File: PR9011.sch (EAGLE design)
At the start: 65 parts, among them J1 M3_SCREW_POST, SW1 SPST_TACT-KMR2, Y1 32.768kHz

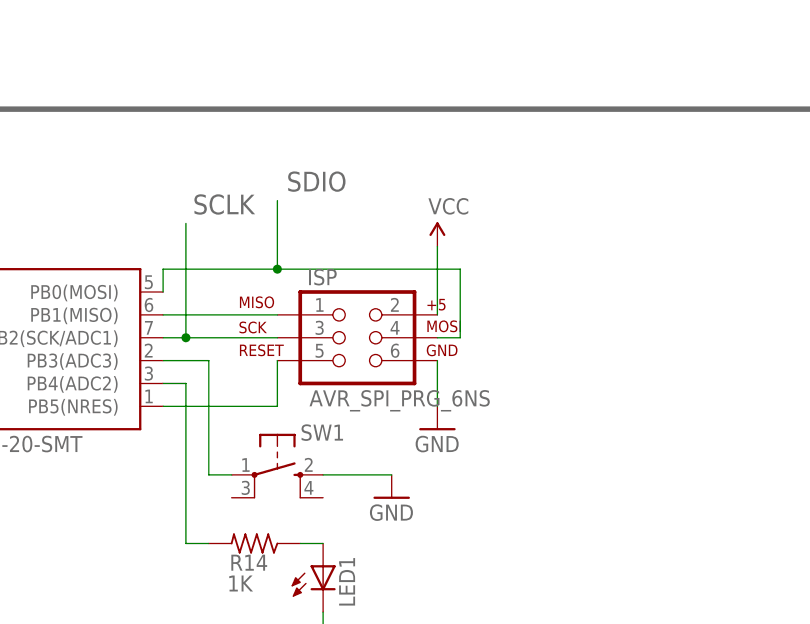
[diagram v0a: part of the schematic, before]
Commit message: Updated SCH
Updated Pullup Resist & Decoupling Vals
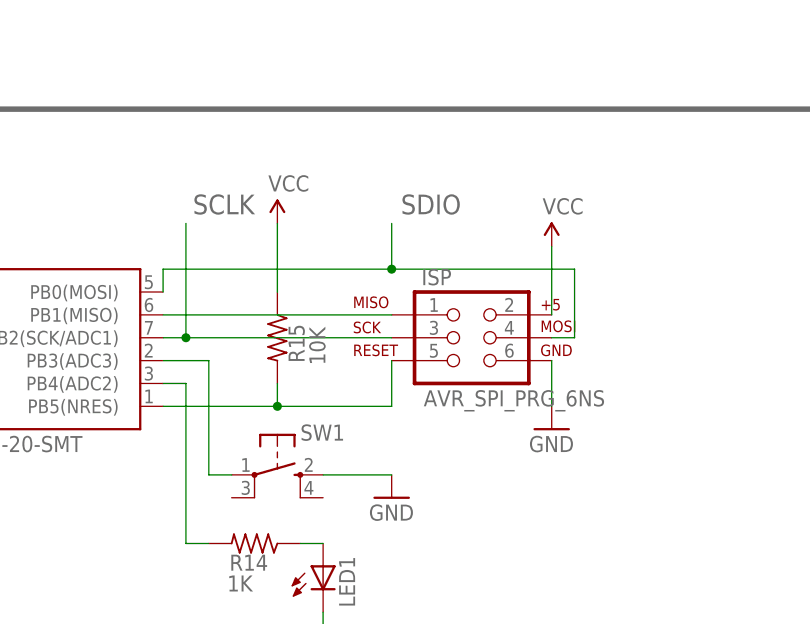
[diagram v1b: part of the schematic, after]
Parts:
- added R15: 10K, resistor:R-US_R0603
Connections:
- net PB5: now also R15.2
- net VCC: now also R15.1
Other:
- moved on the sheet: ISP
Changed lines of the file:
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@@
 <part name="VARI" library="coilcraft-trimmer" deviceset="L-TRIM" device=""/>
 <part name="GND33" library="SparkFun-Aesthetics" deviceset="GND" device=""/>
+<part name="R15" library="resistor" deviceset="R-US_" device="R0603" value="10K"/>
+<part name="SUPPLY1" library="SparkFun-Aesthetics" deviceset="VCC" device=""/>
 </parts>
 <sheets>
@@
 <attribute name="NAME" x="226.06" y="34.798" size="1.778" layer="95" rot="R180"/>
 </instance>
-<instance part="ISP" gate="G$1" x="208.28" y="127"/>
+<instance part="ISP" gate="G$1" x="220.98" y="127"/>
 <instance part="LED1" gate="G$1" x="205.74" y="101.6"/>
 <instance part="GND30" gate="1" x="205.74" y="91.44"/>
-<instance part="SUPPLY9" gate="G$1" x="218.44" y="137.16"/>
-<instance part="GND32" gate="1" x="218.44" y="116.84"/>
+<instance part="SUPPLY9" gate="G$1" x="231.14" y="137.16"/>
+<instance part="GND32" gate="1" x="231.14" y="116.84"/>
 <instance part="R14" gate="G$1" x="198.12" y="104.14" smashed="yes" rot="R180">
 <attribute name="NAME" x="195.326" y="101.1174" size="1.778" layer="95"/>
@@
 <instance part="VARI" gate="G$1" x="17.78" y="25.4"/>
 <instance part="GND33" gate="1" x="17.78" y="15.24"/>
+<instance part="R15" gate="G$1" x="200.66" y="127" smashed="yes" rot="R270">
+<attribute name="NAME" x="203.6826" y="124.206" size="1.778" layer="95" rot="R90"/>
+<attribute name="VALUE" x="205.994" y="123.952" size="1.778" layer="96" rot="R90"/>
+</instance>
+<instance part="SUPPLY1" gate="G$1" x="200.66" y="139.7"/>
 </instances>
 <busses>
@@
 <segment>
 <pinref part="ISP" gate="G$1" pin="6"/>
-<wire x1="218.44" y1="124.46" x2="218.44" y2="119.38" width="0.1524" layer="91"/>
+<wire x1="231.14" y1="124.46" x2="231.14" y2="119.38" width="0.1524" layer="91"/>
 <pinref part="GND32" gate="1" pin="GND"/>
 </segment>
@@
 <pinref part="MCU" gate="G$1" pin="PB2(SCK/ADC1)"/>
 <pinref part="ISP" gate="G$1" pin="3"/>
-<wire x1="200.66" y1="127" x2="190.5" y2="127" width="0.1524" layer="91"/>
+<wire x1="213.36" y1="127" x2="190.5" y2="127" width="0.1524" layer="91"/>
 <label x="191.262" y="140.716" size="2.1844" layer="95"/>
 <wire x1="190.5" y1="127" x2="187.96" y2="127" width="0.1524" layer="91"/>
@@
 </segment>
 <segment>
-<wire x1="220.98" y1="134.62" x2="220.98" y2="127" width="0.1524" layer="91"/>
+<wire x1="233.68" y1="134.62" x2="233.68" y2="127" width="0.1524" layer="91"/>
 <pinref part="ISP" gate="G$1" pin="4"/>
-<wire x1="220.98" y1="127" x2="218.44" y2="127" width="0.1524" layer="91"/>
-<label x="201.676" y="143.256" size="2.1844" layer="95"/>
+<wire x1="233.68" y1="127" x2="231.14" y2="127" width="0.1524" layer="91"/>
+<label x="214.376" y="140.716" size="2.1844" layer="95"/>
 <pinref part="MCU" gate="G$1" pin="PB0(MOSI)"/>
-<wire x1="220.98" y1="134.62" x2="200.66" y2="134.62" width="0.1524" layer="91"/>
-<wire x1="200.66" y1="134.62" x2="187.96" y2="134.62" width="0.1524" layer="91"/>
+<wire x1="233.68" y1="134.62" x2="213.36" y2="134.62" width="0.1524" layer="91"/>
+<wire x1="213.36" y1="134.62" x2="187.96" y2="134.62" width="0.1524" layer="91"/>
 <wire x1="187.96" y1="134.62" x2="187.96" y2="132.08" width="0.1524" layer="91"/>
-<wire x1="200.66" y1="134.62" x2="200.66" y2="142.24" width="0.1524" layer="91"/>
-<junction x="200.66" y="134.62"/>
+<wire x1="213.36" y1="134.62" x2="213.36" y2="139.7" width="0.1524" layer="91"/>
+<junction x="213.36" y="134.62"/>
 </segment>
 </net>
@@
 <segment>
 <pinref part="ISP" gate="G$1" pin="2"/>
-<wire x1="218.44" y1="137.16" x2="218.44" y2="129.54" width="0.1524" layer="91"/>
+<wire x1="231.14" y1="137.16" x2="231.14" y2="129.54" width="0.1524" layer="91"/>
 <pinref part="SUPPLY9" gate="G$1" pin="VCC"/>
 </segment>
@@
 <pinref part="C14" gate="G$1" pin="1"/>
 <wire x1="139.7" y1="139.7" x2="139.7" y2="137.16" width="0.1524" layer="91"/>
+</segment>
+<segment>
+<pinref part="R15" gate="G$1" pin="1"/>
+<wire x1="200.66" y1="132.08" x2="200.66" y2="139.7" width="0.1524" layer="91"/>
+<pinref part="SUPPLY1" gate="G$1" pin="VCC"/>
 </segment>
 </net>
@@
 <pinref part="ISP" gate="G$1" pin="5"/>
 <wire x1="187.96" y1="119.38" x2="200.66" y2="119.38" width="0.1524" layer="91"/>
-<wire x1="200.66" y1="119.38" x2="200.66" y2="124.46" width="0.1524" layer="91"/>
+<wire x1="200.66" y1="119.38" x2="213.36" y2="119.38" width="0.1524" layer="91"/>
+<wire x1="213.36" y1="119.38" x2="213.36" y2="124.46" width="0.1524" layer="91"/>
+<pinref part="R15" gate="G$1" pin="2"/>
+<wire x1="200.66" y1="121.92" x2="200.66" y2="119.38" width="0.1524" layer="91"/>
+<junction x="200.66" y="119.38"/>
 </segment>
 </net>
@@
 <pinref part="ISP" gate="G$1" pin="1"/>
 <pinref part="MCU" gate="G$1" pin="PB1(MISO)"/>
-<wire x1="187.96" y1="129.54" x2="200.66" y2="129.54" width="0.1524" layer="91"/>
-</segment>
-</net>
+<wire x1="187.96" y1="129.54" x2="213.36" y2="129.54" width="0.1524" layer="91"/>
+</segment>
+</net>

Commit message: Updated SCH
Updated SCH
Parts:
- C10: value 1.0uF -> 22nF
- C11: value 1.0uF -> 4.7uF
- C8: value 1.0uF -> .1uF
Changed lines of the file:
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@@
 <?xml version="1.0" encoding="utf-8"?>
 <!DOCTYPE eagle SYSTEM "eagle.dtd">
-<eagle version="6.6.0">
+<eagle version="7.2.0">
 <drawing>
 <settings>
@@
 <part name="C3" library="SparkFun-Capacitors" deviceset="1.0UF-25V-+80/-20(0805)" device="" value="1.0uF"/>
 <part name="GND21" library="SparkFun" deviceset="GND" device=""/>
-<part name="C8" library="SparkFun-Capacitors" deviceset="1.0UF-25V-+80/-20(0805)" device="" value="1.0uF"/>
-<part name="C10" library="SparkFun-Capacitors" deviceset="1.0UF-25V-+80/-20(0805)" device="" value="1.0uF"/>
-<part name="C11" library="SparkFun-Capacitors" deviceset="1.0UF-25V-+80/-20(0805)" device="" value="1.0uF"/>
+<part name="C8" library="SparkFun-Capacitors" deviceset="1.0UF-25V-+80/-20(0805)" device="" value=".1uF"/>
+<part name="C10" library="SparkFun-Capacitors" deviceset="1.0UF-25V-+80/-20(0805)" device="" value="22nF"/>
+<part name="C11" library="SparkFun-Capacitors" deviceset="1.0UF-25V-+80/-20(0805)" device="" value="4.7uF"/>
 <part name="C7" library="SparkFun-Capacitors" deviceset="1.0UF-25V-+80/-20(0805)" device="" value="1.0uF"/>
 <part name="GND16" library="SparkFun" deviceset="GND" device=""/>

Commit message: Updated SCH
Updated SCH
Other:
- note added: "PUBLIC RADIO PR9011 Development Board"
- note removed: "PUBLIC RADIO PR9010"
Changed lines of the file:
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@@
 <text x="160.02" y="76.2" size="2.54" layer="96">Audio Amplifier </text>
 <text x="157.48" y="144.78" size="2.54" layer="96">MCU</text>
-<text x="-27.94" y="162.56" size="3.81" layer="96">PUBLIC RADIO PR9010</text>
+<text x="-27.94" y="162.56" size="3.81" layer="96">PUBLIC RADIO PR9011
+Development Board </text>
 <text x="77.978" y="147.574" size="2.54" layer="96">GND Pads </text>
 </plain>
@@
 </schematic>
 </drawing>
+<compatibility>
+<note version="6.3" minversion="6.2.2" severity="warning">
+Since Version 6.2.2 text objects can contain more than one line,
+which will not be processed correctly with this version.
+</note>
+</compatibility>
 </eagle>

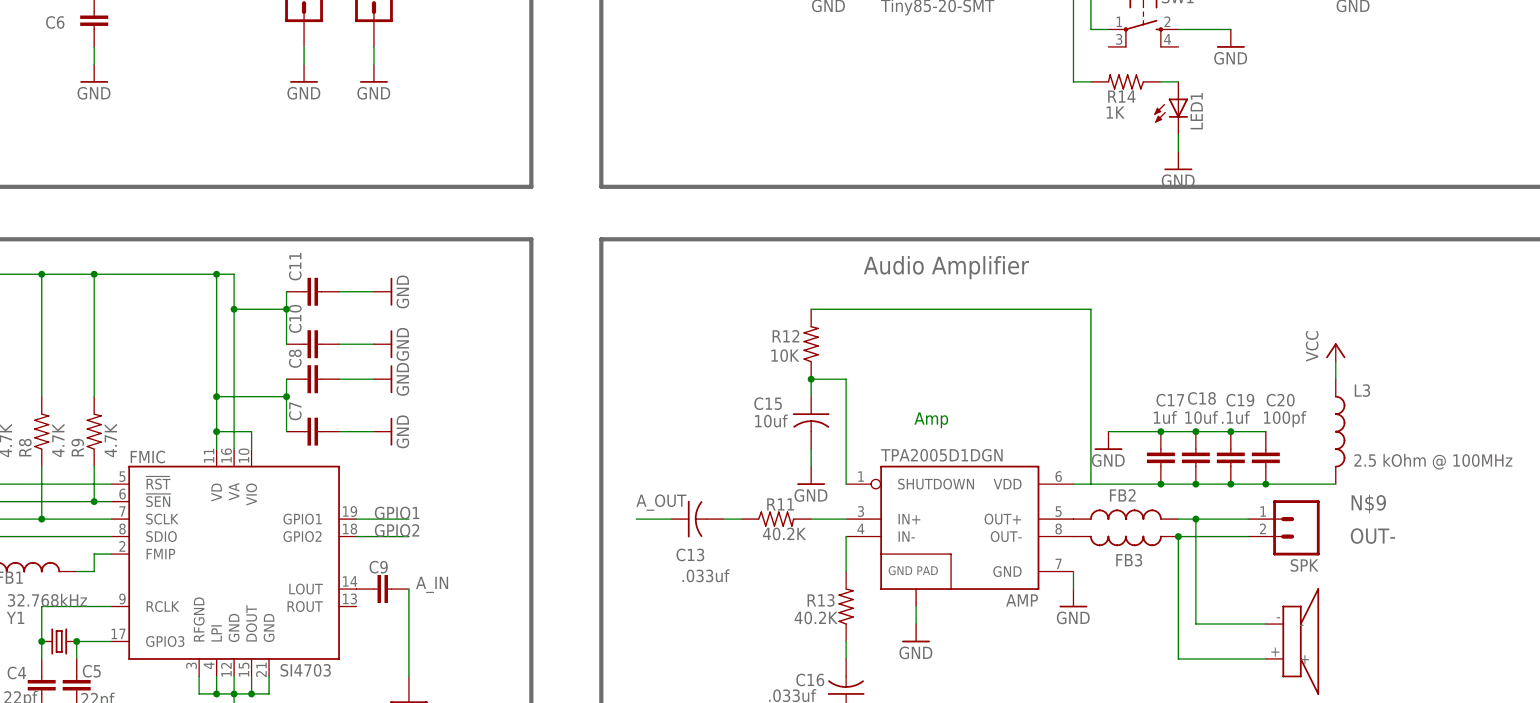
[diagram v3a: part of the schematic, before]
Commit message: Updated SCH
Updated SCH
JST
Fiducials
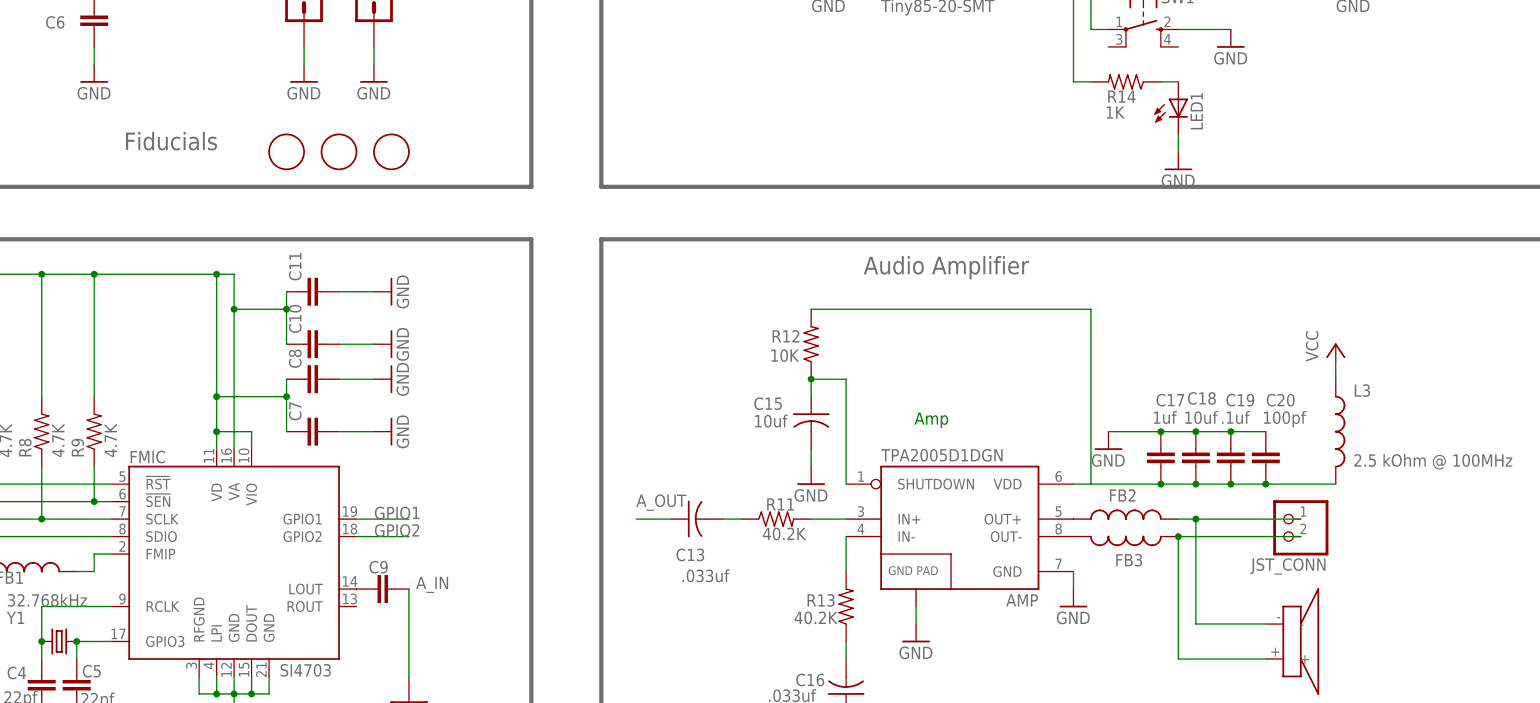
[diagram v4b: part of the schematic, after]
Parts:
- removed SPK: M02PTH3, SparkFun-Connectors:M02PTH3
- added JST_CONN: (no value), adafruit:JST_2PIN-SMT-RA
- added U$1, U$2, U$4: FIDUCIAL, adafruit:FIDUCIAL
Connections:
- net N$9: now also JST_CONN.2; no longer SPK.1
- net OUT-: now also JST_CONN.1; no longer SPK.2
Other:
- note added: "Fiducials"
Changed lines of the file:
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@@
 <?xml version="1.0" encoding="utf-8"?>
 <!DOCTYPE eagle SYSTEM "eagle.dtd">
-<eagle version="7.2.0">
+<eagle version="6.6.0">
 <drawing>
 <settings>
@@
 <part name="SW1" library="adafruit" deviceset="SPST_TACT" device="-KMR2"/>
 <part name="GND31" library="SparkFun" deviceset="GND" device=""/>
-<part name="SPK" library="SparkFun-Connectors" deviceset="M02" device="PTH3"/>
 <part name="ISP" library="SparkFun-Connectors" deviceset="AVR_SPI_PRG_6" device="NS"/>
 <part name="LED1" library="led" deviceset="LED" device="SML0603"/>
@@
 <part name="R15" library="resistor" deviceset="R-US_" device="R0603" value="10K"/>
 <part name="SUPPLY1" library="SparkFun-Aesthetics" deviceset="VCC" device=""/>
+<part name="JST_CONN" library="adafruit" deviceset="JST_2PIN" device="-SMT-RA"/>
+<part name="U$1" library="adafruit" deviceset="FIDUCIAL" device=""/>
+<part name="U$2" library="adafruit" deviceset="FIDUCIAL" device=""/>
+<part name="U$4" library="adafruit" deviceset="FIDUCIAL" device=""/>
 </parts>
 <sheets>
@@
 Development Board </text>
 <text x="77.978" y="147.574" size="2.54" layer="96">GND Pads </text>
+<text x="52.578" y="94.234" size="2.54" layer="96">Fiducials </text>
 </plain>
 <instances>
@@
 </instance>
 <instance part="GND31" gate="1" x="213.36" y="109.22"/>
-<instance part="SPK" gate="G$1" x="223.52" y="40.64" smashed="yes" rot="R180">
-<attribute name="NAME" x="226.06" y="34.798" size="1.778" layer="95" rot="R180"/>
-</instance>
 <instance part="ISP" gate="G$1" x="220.98" y="127"/>
 <instance part="LED1" gate="G$1" x="205.74" y="101.6"/>
@@
 </instance>
 <instance part="SUPPLY1" gate="G$1" x="200.66" y="139.7"/>
+<instance part="JST_CONN" gate="G$1" x="220.98" y="40.64" rot="R180"/>
+<instance part="U$1" gate="G$1" x="91.44" y="93.98"/>
+<instance part="U$2" gate="G$1" x="83.82" y="93.98"/>
+<instance part="U$4" gate="G$1" x="76.2" y="93.98"/>
 </instances>
 <busses>
@@
 <net name="OUT-" class="0">
 <segment>
-<pinref part="SPK" gate="G$1" pin="2"/>
-<label x="230.632" y="37.084" size="2.1844" layer="95"/>
-<wire x1="205.74" y1="38.1" x2="215.9" y2="38.1" width="0.1524" layer="91"/>
 <wire x1="205.74" y1="38.1" x2="205.74" y2="20.32" width="0.1524" layer="91"/>
 <pinref part="U$3" gate="G$1" pin="+"/>
 <wire x1="218.44" y1="20.32" x2="205.74" y2="20.32" width="0.1524" layer="91"/>
 <pinref part="FB3" gate="G$1" pin="1"/>
+<pinref part="JST_CONN" gate="G$1" pin="1"/>
+<wire x1="223.52" y1="38.1" x2="205.74" y2="38.1" width="0.1524" layer="91"/>
 <junction x="205.74" y="38.1"/>
 </segment>
@@
 <net name="N$9" class="0">
 <segment>
-<pinref part="FB2" gate="G$1" pin="2"/>
-<pinref part="SPK" gate="G$1" pin="1"/>
-<wire x1="215.9" y1="40.64" x2="208.28" y2="40.64" width="0.1524" layer="91"/>
-<label x="230.632" y="41.91" size="2.1844" layer="95"/>
 <pinref part="U$3" gate="G$1" pin="-"/>
-<wire x1="208.28" y1="40.64" x2="205.74" y2="40.64" width="0.1524" layer="91"/>
 <wire x1="218.44" y1="25.4" x2="208.28" y2="25.4" width="0.1524" layer="91"/>
 <wire x1="208.28" y1="25.4" x2="208.28" y2="40.64" width="0.1524" layer="91"/>
+<pinref part="FB2" gate="G$1" pin="2"/>
+<wire x1="208.28" y1="40.64" x2="205.74" y2="40.64" width="0.1524" layer="91"/>
+<pinref part="JST_CONN" gate="G$1" pin="2"/>
+<wire x1="208.28" y1="40.64" x2="223.52" y2="40.64" width="0.1524" layer="91"/>
 <junction x="208.28" y="40.64"/>
 </segment>

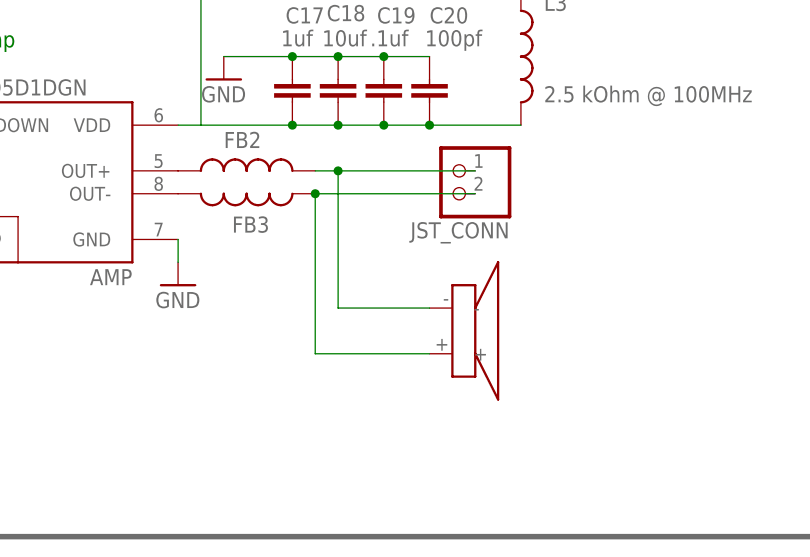
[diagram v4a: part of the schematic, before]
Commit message: changed speaker to JST
added screw holes, removed pads on speaker. re-routed a couple of
traces.
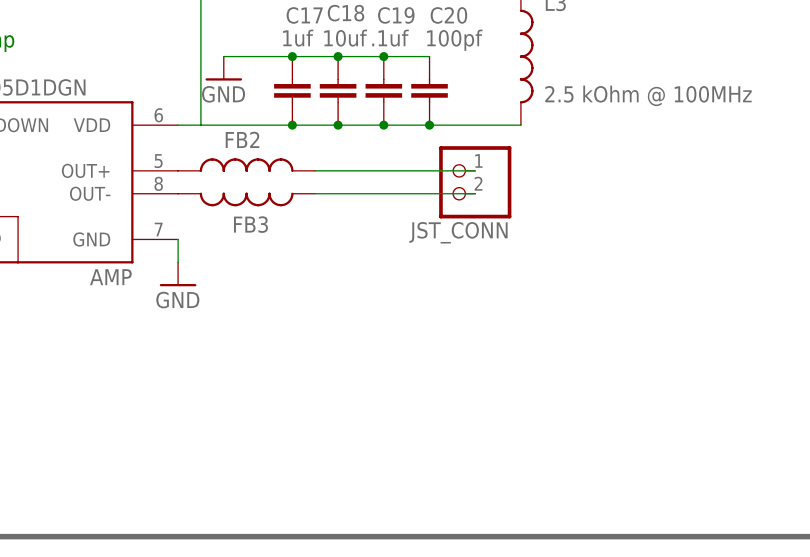
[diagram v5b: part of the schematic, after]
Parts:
- removed U$3: CE32A_DAYTON_SPKR, PR_Libraries:CE32A_DAYTON_SPKR
- added U$5: CE32A_FOR_JST, PR_Libraries:CE32A_FOR_JST
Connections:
- net N$9: no longer U$3.-
- net OUT-: no longer U$3.+
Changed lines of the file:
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@@
 <?xml version="1.0" encoding="utf-8"?>
 <!DOCTYPE eagle SYSTEM "eagle.dtd">
-<eagle version="6.6.0">
+<eagle version="7.2.0">
 <drawing>
 <settings>
@@
 <part name="JP6" library="PR_Libraries" deviceset="BK-92_MPD_AA_BATT_CLIP" device=""/>
 <part name="GND10" library="SparkFun-Aesthetics" deviceset="GND" device=""/>
-<part name="U$3" library="PR_Libraries" deviceset="CE32A_DAYTON_SPKR" device=""/>
 <part name="FB1" library="SparkFun-Passives" deviceset="INDUCTOR" device="0805"/>
 <part name="FB2" library="SparkFun-Passives" deviceset="INDUCTOR" device="0805"/>
@@
 <part name="U$2" library="adafruit" deviceset="FIDUCIAL" device=""/>
 <part name="U$4" library="adafruit" deviceset="FIDUCIAL" device=""/>
+<part name="U$5" library="PR_Libraries" deviceset="CE32A_FOR_JST" device=""/>
 </parts>
 <sheets>
@@
 <instance part="JP6" gate="BATT" x="20.32" y="114.3" rot="R90"/>
 <instance part="GND10" gate="1" x="20.32" y="101.6"/>
-<instance part="U$3" gate="G$1" x="220.98" y="22.86" rot="MR180"/>
 <instance part="FB1" gate="G$1" x="38.1" y="33.02" smashed="yes" rot="R90">
 <attribute name="NAME" x="38.1" y="33.02" size="1.778" layer="95" rot="R180"/>
@@
 <net name="OUT-" class="0">
 <segment>
-<wire x1="205.74" y1="38.1" x2="205.74" y2="20.32" width="0.1524" layer="91"/>
-<pinref part="U$3" gate="G$1" pin="+"/>
-<wire x1="218.44" y1="20.32" x2="205.74" y2="20.32" width="0.1524" layer="91"/>
 <pinref part="FB3" gate="G$1" pin="1"/>
 <pinref part="JST_CONN" gate="G$1" pin="1"/>
 <wire x1="223.52" y1="38.1" x2="205.74" y2="38.1" width="0.1524" layer="91"/>
-<junction x="205.74" y="38.1"/>
 </segment>
 </net>
@@
 <net name="N$9" class="0">
 <segment>
-<pinref part="U$3" gate="G$1" pin="-"/>
-<wire x1="218.44" y1="25.4" x2="208.28" y2="25.4" width="0.1524" layer="91"/>
-<wire x1="208.28" y1="25.4" x2="208.28" y2="40.64" width="0.1524" layer="91"/>
 <pinref part="FB2" gate="G$1" pin="2"/>
-<wire x1="208.28" y1="40.64" x2="205.74" y2="40.64" width="0.1524" layer="91"/>
 <pinref part="JST_CONN" gate="G$1" pin="2"/>
-<wire x1="208.28" y1="40.64" x2="223.52" y2="40.64" width="0.1524" layer="91"/>
-<junction x="208.28" y="40.64"/>
-</segment>
-</net>
+<wire x1="205.74" y1="40.64" x2="223.52" y2="40.64" width="0.1524" layer="91"/>
+</segment>
+</net>
